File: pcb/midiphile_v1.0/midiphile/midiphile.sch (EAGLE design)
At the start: 9 parts

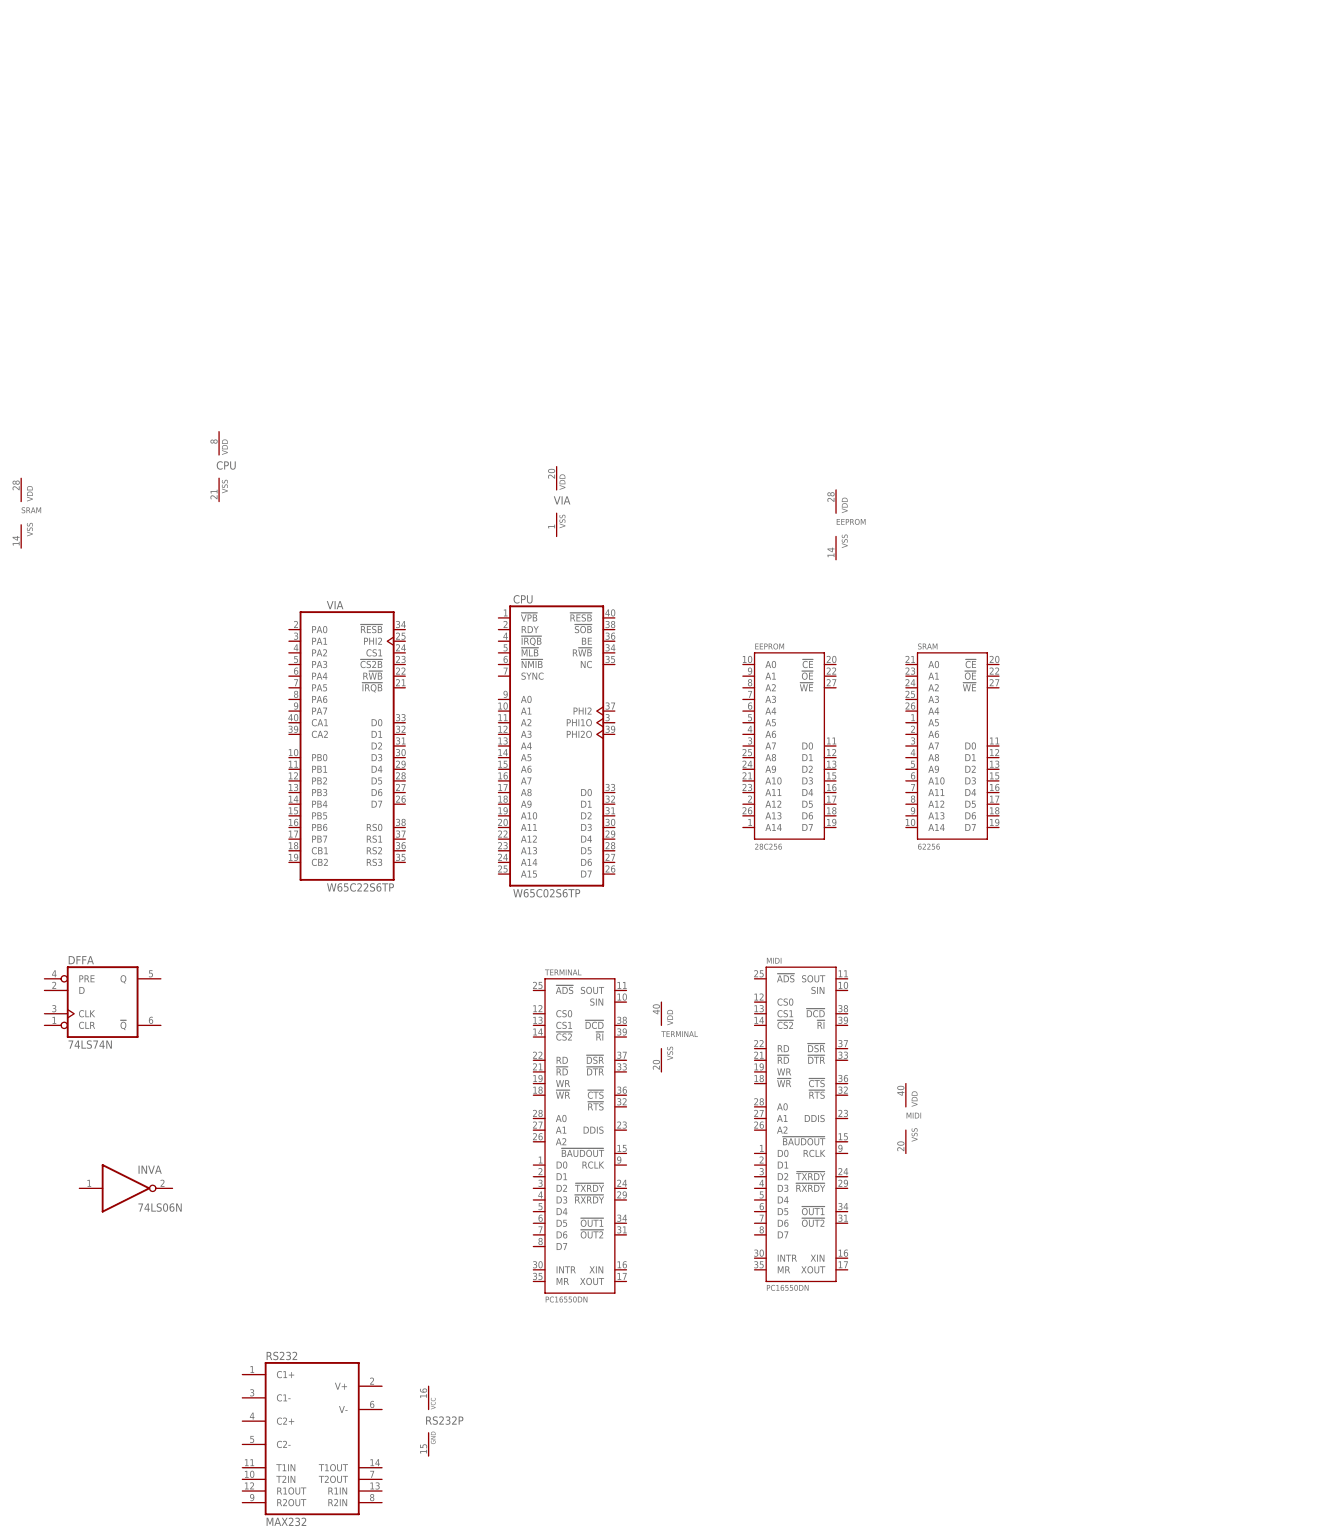
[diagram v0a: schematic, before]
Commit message: Add PLCC packages for 65c02 and 16550; roughly lay out ICs on board
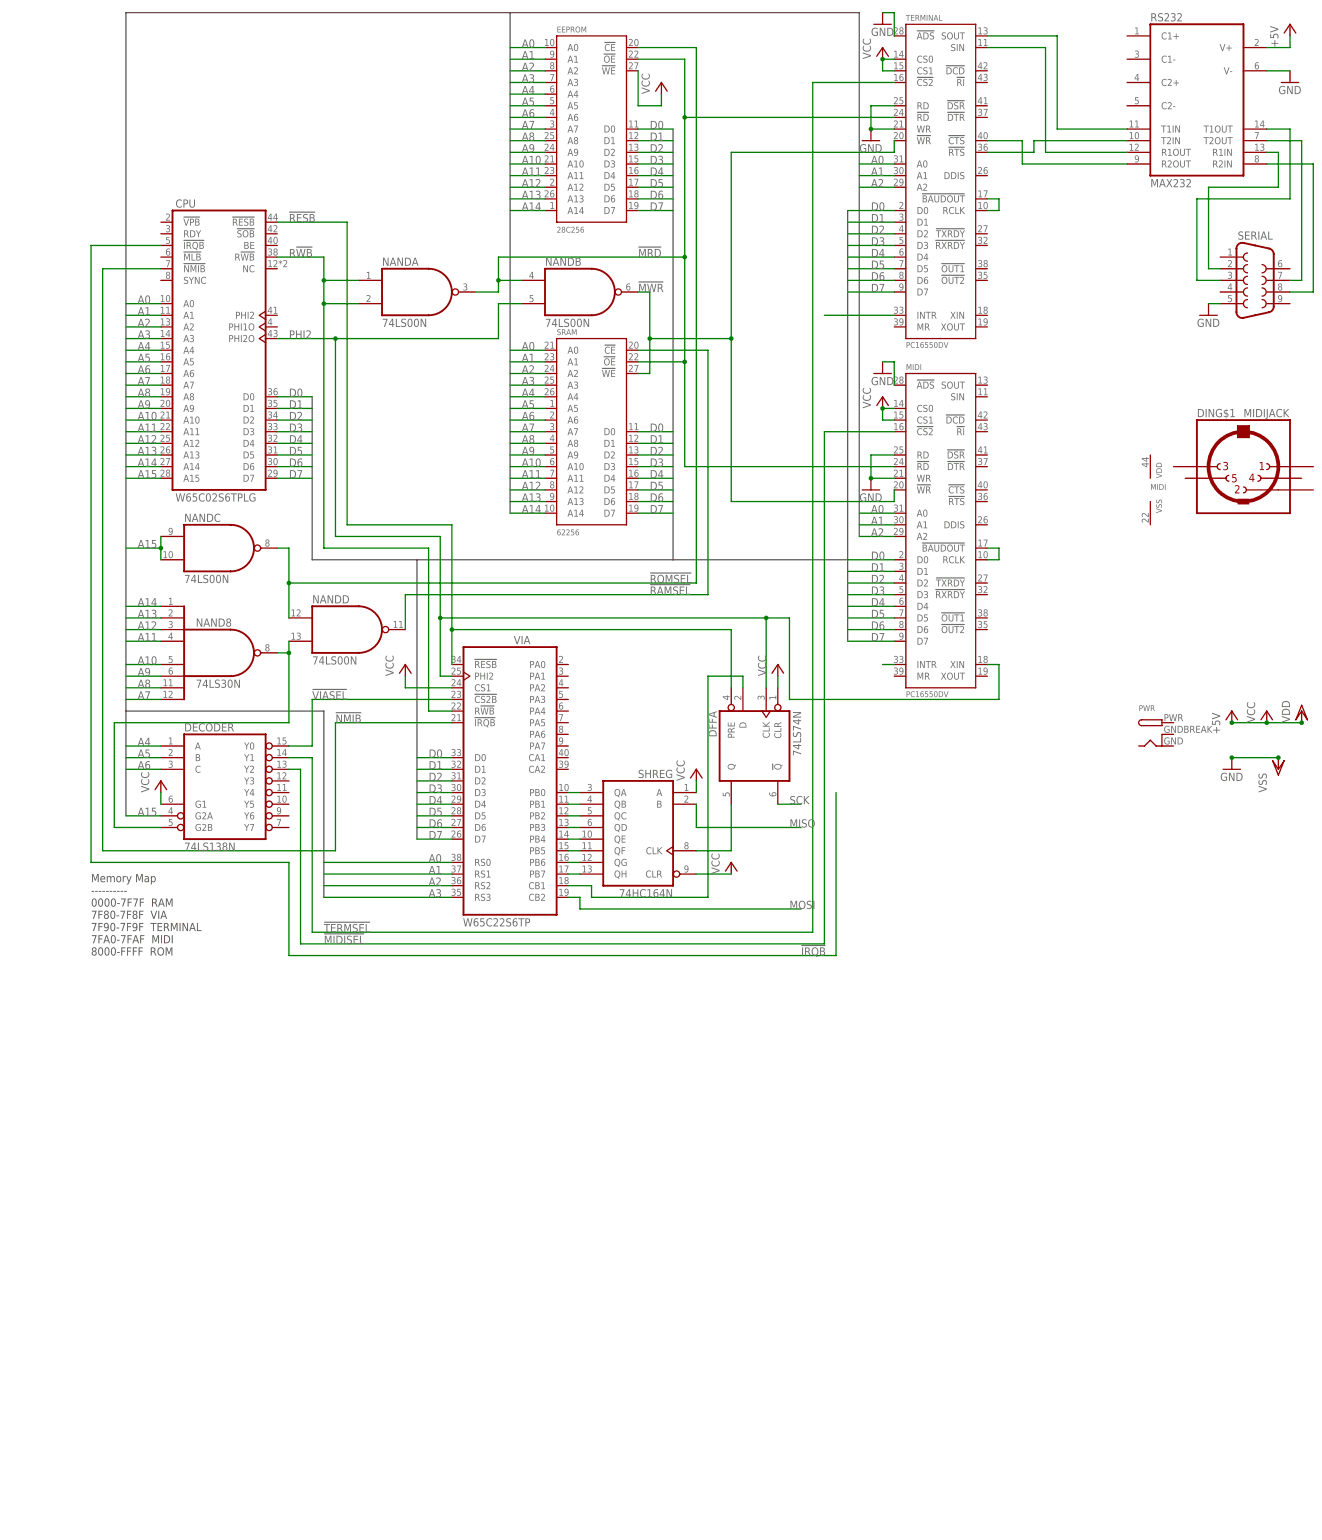
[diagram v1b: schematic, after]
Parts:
- removed INV: 74LS06N, 74xx-us:74LS06N
- added DECODER: 74LS138N, 74xx-us:74LS138N
- added DIN: MIDIJACK, adafruit:MIDIJACK
- added NAND: 74LS00N, 74xx-us:74LS00N
- added NAND8: 74LS30N, 74xx-us:74LS30N
- added PWR: (no value), adafruit:DCBARRELPTH
- added SERIAL: (no value), SparkFun-Connectors:DB9MALE
- added SHREG: 74HC164N, 74xx-us:74HC164N
- CPU: value W65C02S6TP -> W65C02S6TPLG; device 6502:W65C02S6TP -> 6502:W65C02S6TPLG
- MIDI, TERMINAL: value PC16550DN -> PC16550DV; device 16550:PC16550DN -> 16550:PC16550DV
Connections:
- new net !IRQB!: CPUG$1.!IRQB
- new net !MIDISEL!: DECODERA.Y2, MIDIG$1.!CS2!
- new net !MRD!: EEPROMG$1.!OE!, MIDIG$1.!RD!, NANDA.O, NANDB.I0, SRAMG$1.!OE!, TERMINALG$1.!RD!
- new net !MWR!: MIDIG$1.!WR!, NANDB.O, SRAMG$1.!WE!, TERMINALG$1.!WR!
- new net !NMIB!: CPUG$1.!NMIB, VIAVIA.!IRQB
- new net !RAMSEL!: NANDD.O, SRAMG$1.!CE!
- new net !RESB!: CPUG$1.!RESB, DFFA.PRE, VIAVIA.!RESB
- new net !ROMSEL!: EEPROMG$1.!CE!, NANDC.O, NANDD.I0
- new net !TERMSEL!: DECODERA.Y1, TERMINALG$1.!CS2!
- new net !VIASEL!: DECODERA.Y0, VIAVIA.!CS2B
- new net +5V: RS232G$1.V+
- new net A0: CPUG$1.A0, EEPROMG$1.A0, MIDIG$1.A0, SRAMG$1.A0, TERMINALG$1.A0, VIAVIA.RS0
- new net A1: CPUG$1.A1, EEPROMG$1.A1, MIDIG$1.A1, SRAMG$1.A1, TERMINALG$1.A1, VIAVIA.RS1
- new net A10: CPUG$1.A10, EEPROMG$1.A10, NAND8A.I4, SRAMG$1.A10
- new net A11: CPUG$1.A11, EEPROMG$1.A11, NAND8A.I3, SRAMG$1.A11
- new net A12: CPUG$1.A12, EEPROMG$1.A12, NAND8A.I2, SRAMG$1.A12
- new net A13: CPUG$1.A13, EEPROMG$1.A13, NAND8A.I1, SRAMG$1.A13
- new net A14: CPUG$1.A14, EEPROMG$1.A14, NAND8A.I0, SRAMG$1.A14
- new net A15: CPUG$1.A15, DECODERA.G2A, NANDC.I0, NANDC.I1
- new net A2: CPUG$1.A2, EEPROMG$1.A2, MIDIG$1.A2, SRAMG$1.A2, TERMINALG$1.A2, VIAVIA.RS2
- new net A3: CPUG$1.A3, EEPROMG$1.A3, SRAMG$1.A3, VIAVIA.RS3
- new net A4: CPUG$1.A4, DECODERA.A, EEPROMG$1.A4, SRAMG$1.A4
- new net A5: CPUG$1.A5, DECODERA.B, EEPROMG$1.A5, SRAMG$1.A5
- new net A6: CPUG$1.A6, DECODERA.C, EEPROMG$1.A6, SRAMG$1.A6
- new net A7: CPUG$1.A7, EEPROMG$1.A7, NAND8A.I7, SRAMG$1.A7
- new net A8: CPUG$1.A8, EEPROMG$1.A8, NAND8A.I6, SRAMG$1.A8
- new net A9: CPUG$1.A9, EEPROMG$1.A9, NAND8A.I5, SRAMG$1.A9
- new net D0: CPUG$1.D0, EEPROMG$1.D0, MIDIG$1.D0, SRAMG$1.D0, TERMINALG$1.D0, VIAVIA.D0
- new net D1: CPUG$1.D1, EEPROMG$1.D1, MIDIG$1.D1, SRAMG$1.D1, TERMINALG$1.D1, VIAVIA.D1
- new net D2: CPUG$1.D2, EEPROMG$1.D2, MIDIG$1.D2, SRAMG$1.D2, TERMINALG$1.D2, VIAVIA.D2
- new net D3: CPUG$1.D3, EEPROMG$1.D3, MIDIG$1.D3, SRAMG$1.D3, TERMINALG$1.D3, VIAVIA.D3
- new net D4: CPUG$1.D4, EEPROMG$1.D4, MIDIG$1.D4, SRAMG$1.D4, TERMINALG$1.D4, VIAVIA.D4
- new net D5: CPUG$1.D5, EEPROMG$1.D5, MIDIG$1.D5, SRAMG$1.D5, TERMINALG$1.D5, VIAVIA.D5
- new net D6: CPUG$1.D6, EEPROMG$1.D6, MIDIG$1.D6, SRAMG$1.D6, TERMINALG$1.D6, VIAVIA.D6
- new net D7: CPUG$1.D7, EEPROMG$1.D7, MIDIG$1.D7, SRAMG$1.D7, TERMINALG$1.D7, VIAVIA.D7
- new net GND: MIDIG$1.!ADS!, MIDIG$1.RD, MIDIG$1.WR, RS232G$1.V-, SERIAL.5, TERMINALG$1.!ADS!, TERMINALG$1.RD, TERMINALG$1.WR
- new net MISO: SHREGA.B
- new net MOSI: VIAVIA.CB2
- new net N$10: SHREGA.QD, VIAVIA.PB3
- new net N$11: SHREGA.QE, VIAVIA.PB4
- new net N$12: SHREGA.QF, VIAVIA.PB5
- new net N$13: SHREGA.QG, VIAVIA.PB6
- new net N$14: SHREGA.QH, VIAVIA.PB7
- new net N$15: DFFA.D, VIAVIA.CB1
- new net N$16: RS232G$1.T1IN, TERMINALG$1.SOUT
- new net N$17: DFFA.Q, SHREGA.CLK
- new net N$18: RS232G$1.R1OUT, TERMINALG$1.SIN
- new net N$19: RS232G$1.T2IN, TERMINALG$1.!RTS!
- new net N$2: DECODERA.G2B, NAND8A.O, NANDD.I1
- new net N$20: RS232G$1.R2OUT, TERMINALG$1.!CTS!
- new net N$21: RS232G$1.T1OUT, SERIAL.3
- new net N$22: RS232G$1.R1IN, SERIAL.2
- new net N$23: RS232G$1.T2OUT, SERIAL.7
- new net N$24: RS232G$1.R2IN, SERIAL.8
- new net N$3: MIDIG$1.INTR
- new net N$4: TERMINALG$1.INTR
- new net N$5: MIDIG$1.!BAUDOUT!, MIDIG$1.RCLK
- new net N$6: TERMINALG$1.!BAUDOUT!, TERMINALG$1.RCLK
- new net N$7: SHREGA.QA, VIAVIA.PB0
- new net N$8: SHREGA.QB, VIAVIA.PB1
- new net N$9: SHREGA.QC, VIAVIA.PB2
- new net PHI2: CPUG$1.PHI2O, DFFA.CLK, MIDIG$1.XIN, NANDB.I1, VIAVIA.PHI2
- new net R!WB!: CPUG$1.R!WB, NANDA.I0, NANDA.I1, VIAVIA.R!WB
- new net SCK: DFFA.!Q
- new net VCC: DECODERA.G1, DFFA.CLR, EEPROMG$1.!WE!, MIDIG$1.CS0, MIDIG$1.CS1, SHREGA.A, SHREGA.CLR, TERMINALG$1.CS0, TERMINALG$1.CS1, VIAVIA.CS1
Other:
- note added: "Memory Map ---------- 0000-7F7F RAM 7F80-7F8F VIA 7F90-7F9F TERMINAL 7FA0-7FAF MIDI 8000-FFFF ROM"
- moved on the sheet: DFFA, EEPROM, MIDI, RS232, SRAM, TERMINAL, VIA

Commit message: Add oscillators, reset and nmi, and thinner sram
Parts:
- added NMI, RES: SWITCH-MOMENTARY-2PTH, SparkFun-Electromechanical:SWITCH-MOMENTARY-2PTH
- added NMIMON, RSTMON: DS1813, ds1813:DS1813
- added SERCLK: 1.8432M, metal_can_oscillator:HALF_CAN_OSC
- added SYSCLK: 1M, metal_can_oscillator:HALF_CAN_OSC
- PWR: value (none) -> USB-MB-H; device adafruit:DCBARRELPTH -> SparkFun-Connectors:USB-MB-H
- SRAM: value 62256 -> 71256SA20TPG; device 62xxx_sram:62256 -> 71xxx_sram:71256SA20TPG
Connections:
- removed net !NMIB!: CPUG$1.!NMIB, VIAVIA.!IRQB
- new net N$1: CPUG$1.!NMIB, NMI.2, NMIMON.!RST!
- new net N$25: SERCLK.OUT, TERMINALG$1.XIN
- net !IRQB!: now also VIAVIA.!IRQB
- net !RESB!: now also RES.1, RSTMON.!RST!
- net GND: now also NMI.1, NMIMON.GND, RES.2, RSTMON.GND, SERCLK.GND, SYSCLK.GND
- net PHI2: now also CPUG$1.PHI2, SYSCLK.OUT; no longer CPUG$1.PHI2O
- net VCC: now also NMIMON.VCC, RSTMON.VCC, SERCLK.VCC, SYSCLK.VCC
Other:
- moved on the sheet: CPU
